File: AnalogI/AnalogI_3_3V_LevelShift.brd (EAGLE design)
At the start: 64 x 82 mm, 80 parts, among them IC1 HCPL-7800, IC2 HCPL-7800, IC3 HCPL-7800, IC4 HCPL-7800, IC5 MCP3424SOIC, IC6 74HC4051_MUXN, IC7 74HC4051_MUXN, P1 DF11-06-2DSA, Q1 BS170, Q2 BS170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

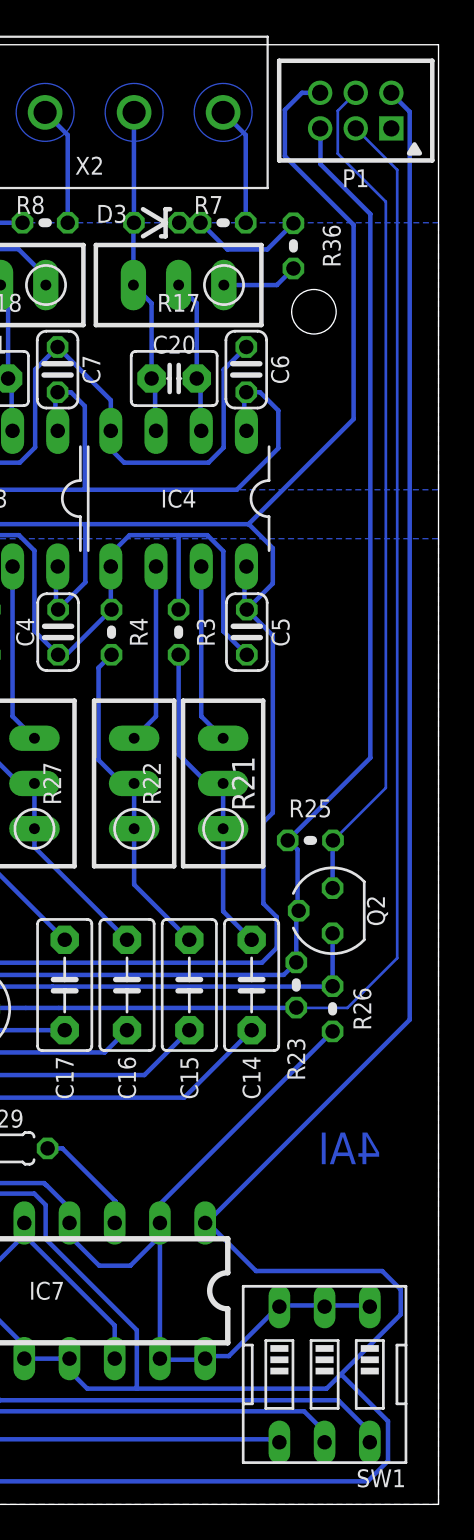
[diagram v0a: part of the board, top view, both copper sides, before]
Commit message: Change wire width from 6 to 8 mil.
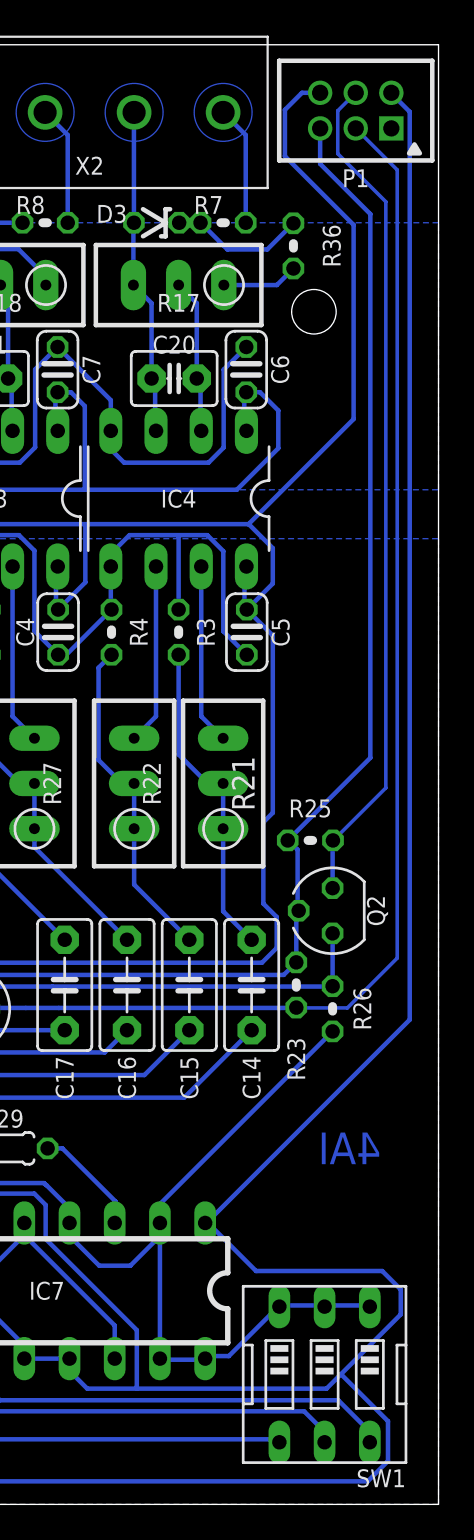
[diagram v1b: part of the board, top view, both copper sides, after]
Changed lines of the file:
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@@
 <wire x1="47.05" y1="9.79" x2="47.05" y2="6.62" width="0.254" layer="16"/>
 <wire x1="47.05" y1="6.62" x2="47.05" y2="6.6024" width="0.254" layer="16"/>
-<wire x1="47.06" y1="6.62" x2="47.05" y2="6.62" width="0.1524" layer="16"/>
-<wire x1="47.06" y1="6.62" x2="47.06" y2="6.5024" width="0.1524" layer="16"/>
+<wire x1="47.06" y1="6.62" x2="47.05" y2="6.62" width="0.203" layer="16"/>
+<wire x1="47.06" y1="6.62" x2="47.06" y2="6.5024" width="0.203" layer="16"/>
 <wire x1="61.1632" y1="4.6736" x2="61.1632" y2="2.4384" width="0.254" layer="16"/>
 <wire x1="58.5216" y1="7.3152" x2="61.1632" y2="4.6736" width="0.254" layer="16"/>
@@
 <contactref element="Q2" pad="G"/>
 <contactref element="R25" pad="2"/>
-<wire x1="57.3024" y1="77.216" x2="57.35" y2="77.3" width="0.254" layer="16"/>
 <wire x1="56.0832" y1="36.7792" x2="56.0832" y2="33.528" width="0.254" layer="16"/>
 <wire x1="55.6768" y1="37.1856" x2="56.0832" y2="36.7792" width="0.254" layer="16"/>
@@
 <wire x1="37.5" y1="29.745" x2="55.305" y2="29.745" width="0.254" layer="16"/>
 <wire x1="55.305" y1="29.745" x2="56.01" y2="30.45" width="0.254" layer="16"/>
-<wire x1="57.32" y1="77.3" x2="57.35" y2="77.3" width="0.254" layer="16"/>
-<wire x1="57.33" y1="77.3" x2="57.35" y2="77.3" width="0.254" layer="16"/>
-<wire x1="57.35" y1="77.3" x2="57.37" y2="77.28" width="0.254" layer="16"/>
-<wire x1="57.37" y1="77.28" x2="57.37" y2="75.29" width="0.254" layer="16"/>
-<wire x1="57.37" y1="75.29" x2="60.17" y2="72.49" width="0.254" layer="16"/>
 <wire x1="60.17" y1="72.49" x2="60.17" y2="41.94" width="0.254" layer="16"/>
 <wire x1="60.17" y1="41.94" x2="55.53" y2="37.3" width="0.254" layer="16"/>
@@
 <wire x1="56.01" y1="33.4548" x2="56.01" y2="33.36" width="0.254" layer="16"/>
 <wire x1="56.01" y1="33.36" x2="56.01" y2="30.45" width="0.254" layer="16"/>
-<wire x1="56.12" y1="33.36" x2="56.14" y2="33.36" width="0.1524" layer="16"/>
-<wire x1="56.14" y1="33.36" x2="56.145" y2="33.35" width="0.1524" layer="16"/>
-<wire x1="56.12" y1="33.36" x2="56.01" y2="33.36" width="0.1524" layer="16"/>
+<wire x1="56.12" y1="33.36" x2="56.14" y2="33.36" width="0.203" layer="16"/>
+<wire x1="56.14" y1="33.36" x2="56.145" y2="33.35" width="0.203" layer="16"/>
+<wire x1="56.12" y1="33.36" x2="56.01" y2="33.36" width="0.203" layer="16"/>
+<wire x1="57.35" y1="77.3" x2="57.35" y2="75.31" width="0.254" layer="16"/>
+<wire x1="57.35" y1="75.31" x2="60.17" y2="72.49" width="0.254" layer="16"/>
 </signal>
 <signal name="+5V">
@@
 <contactref element="Q1" pad="S"/>
 <contactref element="P1" pad="3"/>
-<wire x1="55.9308" y1="27.8892" x2="56.01" y2="27.91" width="0.1524" layer="16"/>
-<wire x1="59.2836" y1="77.2668" x2="59.35" y2="77.3" width="0.1524" layer="16"/>
+<wire x1="55.9308" y1="27.8892" x2="56.01" y2="27.91" width="0.203" layer="16"/>
+<wire x1="59.2836" y1="77.2668" x2="59.35" y2="77.3" width="0.203" layer="16"/>
 <wire x1="42.672" y1="27.8892" x2="55.9892" y2="27.8892" width="0.254" layer="16"/>
 <wire x1="55.9892" y1="27.8892" x2="56.01" y2="27.91" width="0.254" layer="16"/>
-<wire x1="56.01" y1="27.91" x2="56.03" y2="27.89" width="0.1524" layer="16"/>
-<wire x1="56.03" y1="27.89" x2="58.88" y2="27.89" width="0.1524" layer="16"/>
-<wire x1="59.35" y1="77.3" x2="61.68" y2="74.97" width="0.1524" layer="16"/>
-<wire x1="61.68" y1="74.97" x2="61.68" y2="30.69" width="0.1524" layer="16"/>
-<wire x1="61.68" y1="30.69" x2="58.88" y2="27.89" width="0.1524" layer="16"/>
+<wire x1="56.01" y1="27.91" x2="56.03" y2="27.89" width="0.203" layer="16"/>
+<wire x1="56.03" y1="27.89" x2="58.88" y2="27.89" width="0.203" layer="16"/>
+<wire x1="59.35" y1="77.3" x2="61.68" y2="74.97" width="0.203" layer="16"/>
+<wire x1="61.68" y1="74.97" x2="61.68" y2="30.69" width="0.203" layer="16"/>
+<wire x1="61.68" y1="30.69" x2="58.88" y2="27.89" width="0.203" layer="16"/>
 <wire x1="40.8192" y1="27.8892" x2="42.672" y2="27.8892" width="0.254" layer="16"/>
 <wire x1="40.8192" y1="27.8892" x2="38.8192" y2="27.8892" width="0.254" layer="16"/>
@@
 <contactref element="P1" pad="4"/>
 <wire x1="58.1152" y1="37.1856" x2="58.07" y2="37.3" width="0.254" layer="16"/>
-<wire x1="59.35" y1="79.3" x2="58.34" y2="78.29" width="0.1524" layer="16"/>
-<wire x1="58.34" y1="78.29" x2="58.34" y2="75.88" width="0.1524" layer="16"/>
+<wire x1="59.35" y1="79.3" x2="58.34" y2="78.29" width="0.203" layer="16"/>
+<wire x1="58.34" y1="78.29" x2="58.34" y2="75.88" width="0.203" layer="16"/>
 <wire x1="58.05" y1="34.62" x2="58.05" y2="37.28" width="0.254" layer="16"/>
 <wire x1="58.05" y1="37.28" x2="58.07" y2="37.3" width="0.254" layer="16"/>
-<wire x1="58.34" y1="75.88" x2="61.04" y2="73.18" width="0.1524" layer="16"/>
-<wire x1="61.04" y1="73.18" x2="61.04" y2="40.25" width="0.1524" layer="16"/>
-<wire x1="61.04" y1="40.25" x2="58.09" y2="37.3" width="0.1524" layer="16"/>
+<wire x1="58.34" y1="75.88" x2="61.04" y2="73.18" width="0.203" layer="16"/>
+<wire x1="61.04" y1="73.18" x2="61.04" y2="40.25" width="0.203" layer="16"/>
+<wire x1="61.04" y1="40.25" x2="58.09" y2="37.3" width="0.203" layer="16"/>
 <wire x1="58.09" y1="37.3" x2="58.07" y2="37.3" width="0.254" layer="16"/>
 </signal>
@@
 <wire x1="56.45" y1="5.23" x2="37.82" y2="5.23" width="0.254" layer="16"/>
 <wire x1="37.82" y1="5.23" x2="35.66" y2="7.39" width="0.254" layer="16"/>
-<wire x1="57.6" y1="4.08" x2="57.6" y2="3.49" width="0.1524" layer="16"/>
+<wire x1="57.6" y1="4.08" x2="57.6" y2="3.49" width="0.203" layer="16"/>
 </signal>
 <signal name="N$48">
